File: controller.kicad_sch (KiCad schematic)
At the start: 40 parts, among them J201 SWD, J202 USB_C_Receptacle_USB2.0_16P, SW201 CL-SB_22A-12T, U201 ULN2803A, U202 IP4234CZ6, U203 STM32G431CBTx, U204 MCP2542FDxMF, U205 ILD74, Y201 24MHz

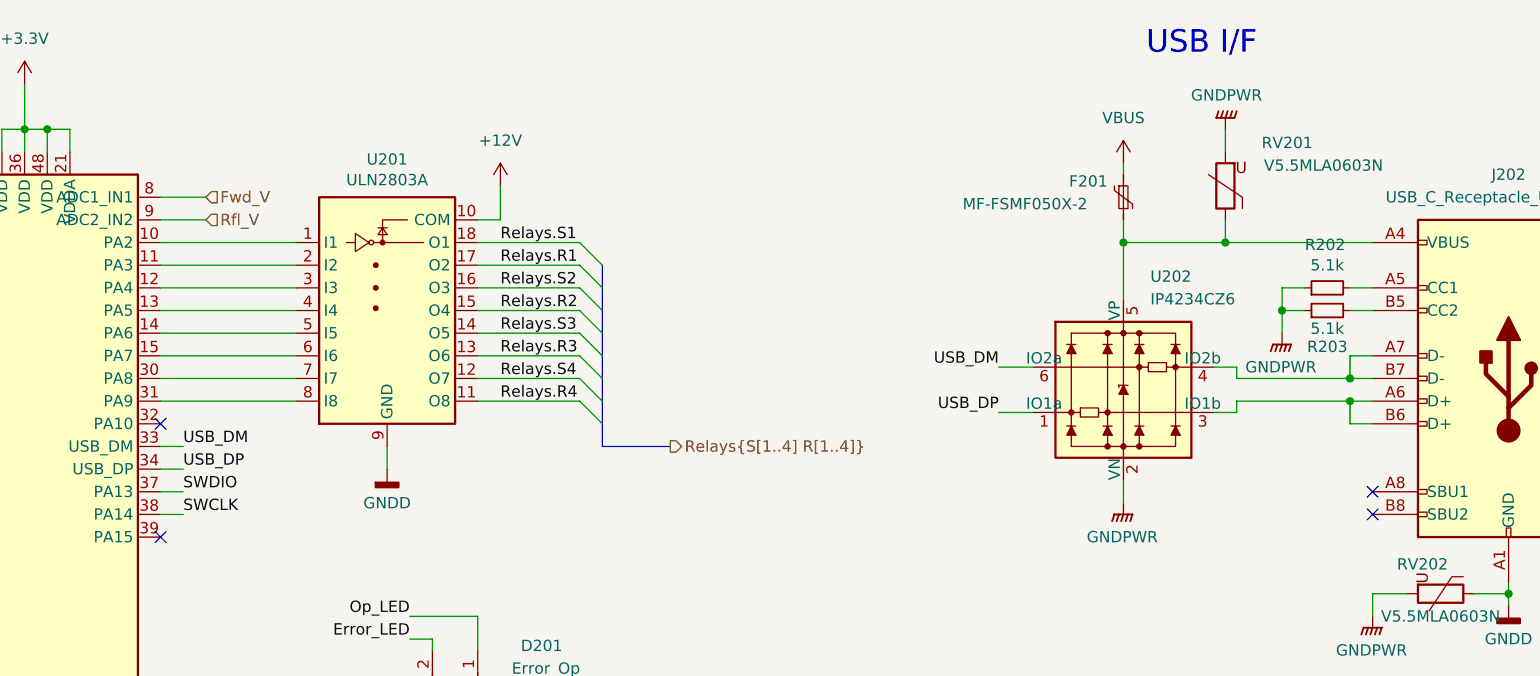
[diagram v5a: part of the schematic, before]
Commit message: Schematic fixes for PCB layout
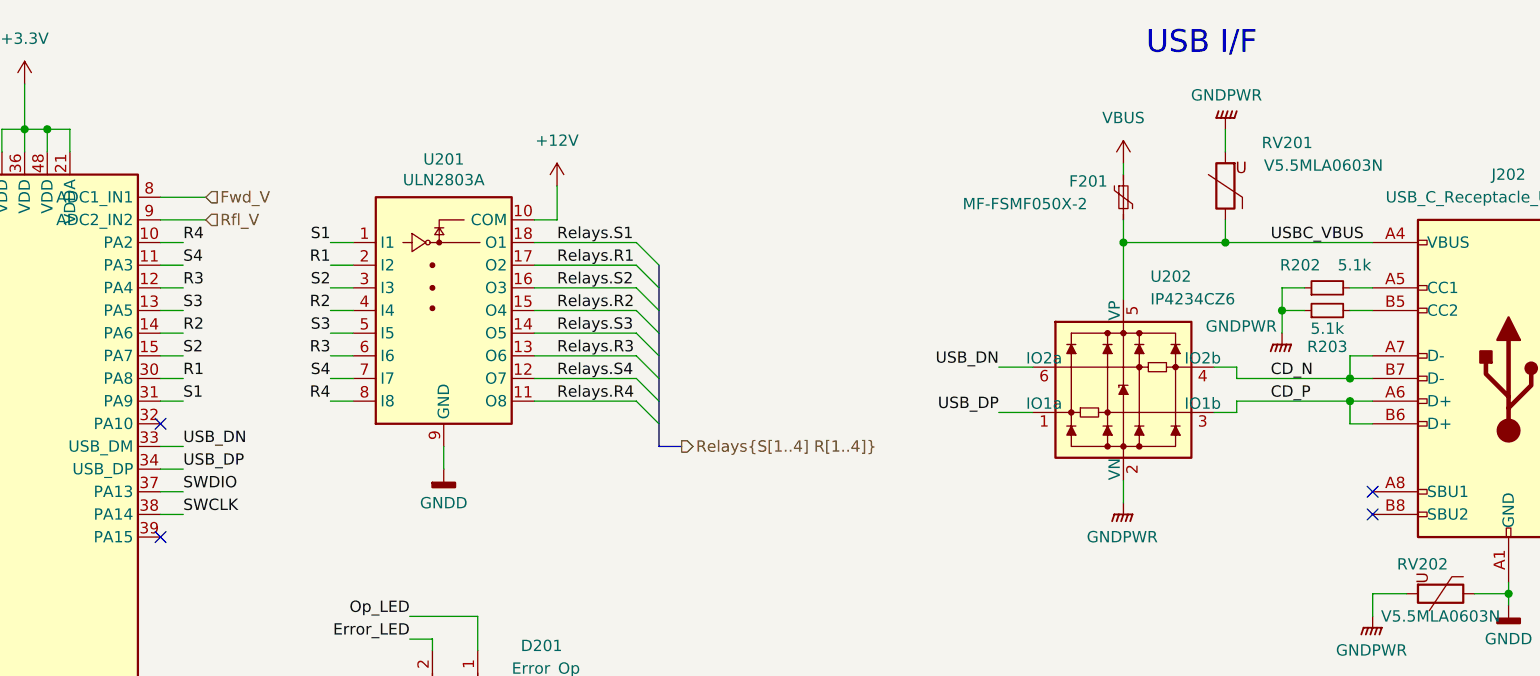
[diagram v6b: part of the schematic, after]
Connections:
- net USBC_VBUS: now reaches F201.2, J202.A4 (VBUS), J202.A9 (VBUS), J202.B4 (VBUS), J202.B9 (VBUS), RV201.1, U202.5 (VP)
- net CD_P: now reaches J202.A6 (D+), J202.B6 (D+), U202.3 (IO1b)
- net CD_N: now reaches J202.A7 (D-), J202.B7 (D-), U202.4 (IO2b)
- net R4: now reaches U203.10 (PA2)
- net R4: now also U201.8 (I8); no longer U201.1 (I1)
- net R1: now reaches U201.2 (I2)
- net R1: now also U203.30 (PA8); no longer U203.11 (PA3)
- net R3: now reaches U203.12 (PA4)
- net R3: now also U201.6 (I6); no longer U201.3 (I3)
- net R2: now reaches U201.4 (I4)
- net R2: now also U203.14 (PA6); no longer U203.13 (PA5)
- net S3: now reaches U201.5 (I5)
- net S3: now also U203.13 (PA5); no longer U203.14 (PA6)
- net S2: now reaches U203.15 (PA7)
- net S2: now also U201.3 (I3); no longer U201.6 (I6)
- net S4: now reaches U201.7 (I7)
- net S4: now also U203.11 (PA3); no longer U203.30 (PA8)
- net S1: now reaches U203.31 (PA9)
- net S1: now also U201.1 (I1); no longer U201.8 (I8)
- net USB_DM renamed USB_DN
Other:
- moved on the sheet: U201
